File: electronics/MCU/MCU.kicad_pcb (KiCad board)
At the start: 2 copper layers, 77.5 x 26 mm, 46 parts, among them J1 UART, J10 Conn_01x09, J11 Button, J12 Power, J2 Conn_01x01, J3 Conn_01x01, J4 Conn_01x01, J5 Conn_01x01, J6 Conn_01x01, J7 Conn_01x01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

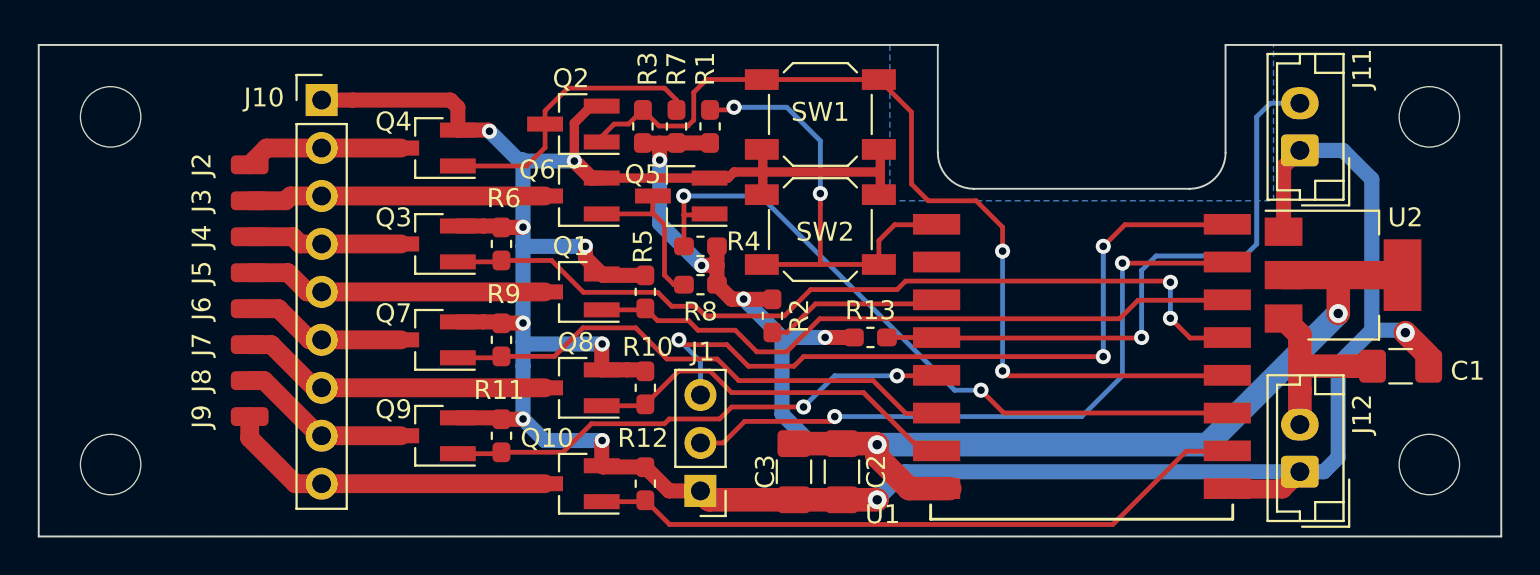
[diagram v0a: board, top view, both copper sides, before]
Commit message: Relay board ready, ESP3266 redesign (GPIO16 instead of GPIO0)
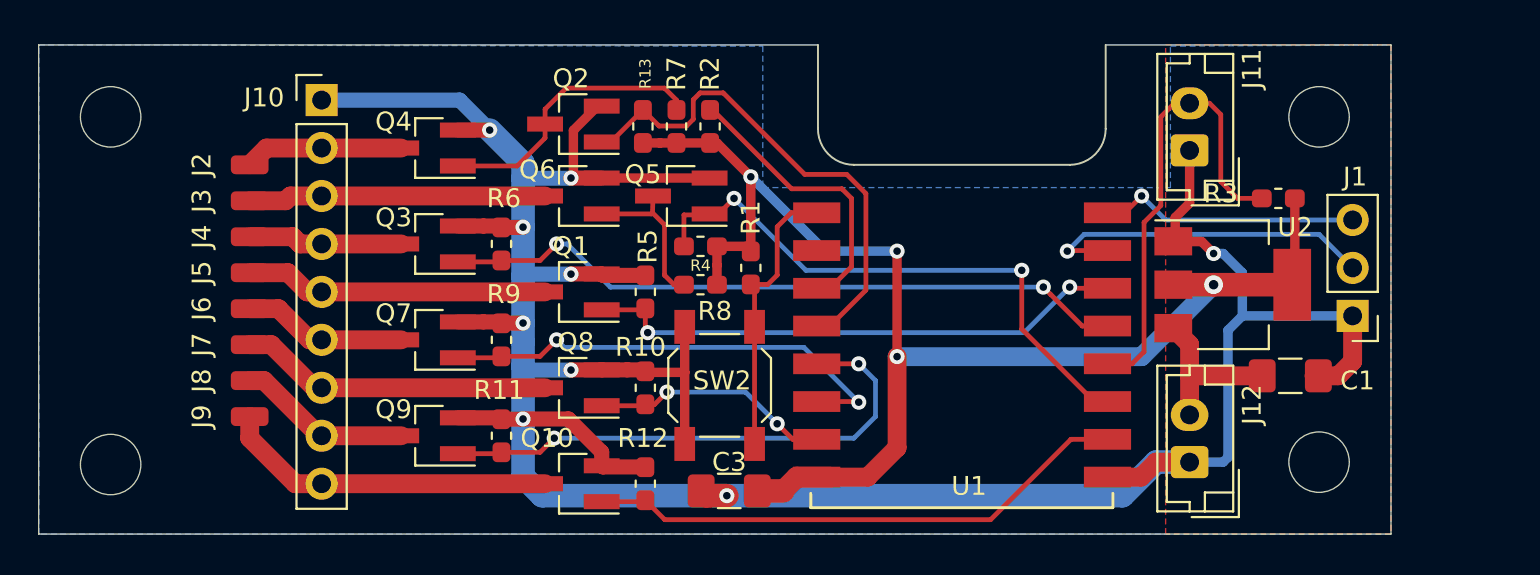
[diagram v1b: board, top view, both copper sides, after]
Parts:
- removed C2: 100n, Capacitor_SMD:C_1206_3216Metric_Pad1.42x1.75mm_HandSolder
- removed SW1: Flash, Button_Switch_SMD:SW_SPST_SKQG_WithStem
- R13: value 1k -> 10k
- R7, R8: value 1k -> 3k3
- moved J1 35.8 mm to (85.1, 75.6)
- moved R3 33.9 mm to (81.2, 69.3), turned to 180 degrees
- moved R13 16.4 mm to (47.5, 65.5), turned to 90 degrees
- moved R2 10.6 mm to (51.1, 65.5), turned to 90 degrees
- moved SW2 9.83 mm to (51.6, 79.2), turned to 270 degrees
- moved R1 7.80 mm to (53.2, 73.0), turned to 270 degrees
- moved U1 6.38 mm to (57.4, 70.1)
- moved J12 5.86 mm to (76.5, 83.3)
- moved C1 5.86 mm to (81.8, 78.7)
- moved U2 5.86 mm to (78.7, 73.9)
- moved REF** 5.84 mm to (83.3, 83.3)
- moved J11 5.84 mm to (76.5, 66.8)
- moved REF** 5.84 mm to (83.3, 65.0)
- moved C3 3.58 mm to (52.1, 84.8), turned to 180 degrees
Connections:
- net Net-(R1-Pad2) renamed /RST
- J11 pad 2: Net-(J11-Pad2) -> /GPIO0
- Q2 pad 1: /GPIO0 -> /GPIO16
- R13 pad 2: Net-(J11-Pad2) -> /GPIO16
- U1 pad 4: Net-(J11-Pad2) -> /GPIO16
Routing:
- net Net-(J11-Pad2): track 33.1 -> 0.00 mm, vias 1 -> 0
- net /GPIO16: track 0.00 -> 26.4 mm
- net Net-(J1-Pad3): track 38.8 -> 14.6 mm, vias 3 -> 1
- net /GPIO0: track 48.7 -> 25.5 mm, vias 2 -> 0
- net Net-(J1-Pad2): track 34.7 -> 17.7 mm, vias 2 -> 1
- net /RST: track 24.8 -> 15.8 mm, vias 2 -> 0
- net /GPIO4: track 44.4 -> 35.9 mm
- net /GPIO13: track 21.0 -> 13.4 mm, vias 0 -> 2
- net +3V3: track 78.8 -> 71.8 mm, vias 6 -> 4
- net /GPIO2: track 36.9 -> 30.0 mm
- net /GPIO15: track 34.6 -> 28.3 mm
- net /GPIO5: track 34.6 -> 28.4 mm, vias 0 -> 2
- net Net-(R2-Pad2): track 10.1 -> 14.7 mm
- net /GPIO12: track 28.6 -> 24.5 mm, vias 0 -> 2
- net /5V_In: track 9.82 -> 8.80 mm
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- added copper zone on F.Cu, net GND
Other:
- board size 77.5 x 26 mm -> 71.6 x 25.9 mm
- net class GND: trace_width 0.8 -> 0.5
- net class Power: trace_width 0.8 -> 0.5

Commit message: MCU: GPIO3 instead if GPIO2
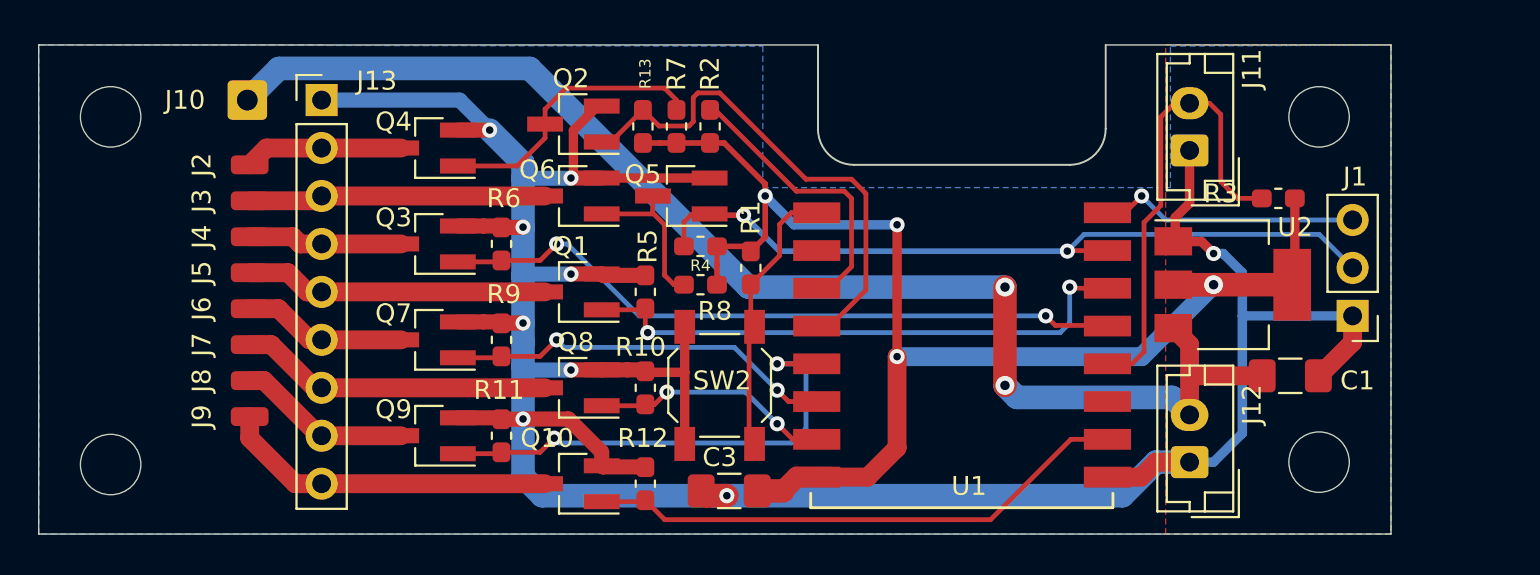
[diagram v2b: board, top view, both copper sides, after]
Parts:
- added J13: Relay +5V, Connector_Wire:SolderWire-0.5sqmm_1x01_D0.9mm_OD2.1mm, F.Cu at (26.5, 64.1)
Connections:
- net Net-(J1-Pad3) renamed /GPIO1
- J1 pad 2: Net-(J1-Pad2) -> /GPIO3
- Q5 pad 1: /GPIO2 -> /GPIO3
- R4 pad 2: /GPIO2 -> /GPIO3
- U1 pad 11: /GPIO2 -> (no net)
- U1 pad 15: Net-(J1-Pad2) -> /GPIO3
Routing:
- net /5V_In: track 8.80 -> 69.8 mm, vias 0 -> 2
- net /GPIO3: track 0.00 -> 40.3 mm, vias 0 -> 2
- net /GPIO2: track 30.0 -> 0.00 mm, vias 2 -> 0
- net Net-(J1-Pad2): track 17.7 -> 0.00 mm, vias 1 -> 0
- net /GPIO12: track 24.5 -> 21.5 mm
- net GND: track 160.6 -> 159.3 mm
- net /GPIO5: track 28.4 -> 29.5 mm
- net /GPIO14: track 27.6 -> 26.9 mm

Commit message: Small PCB modifications, esphome config added
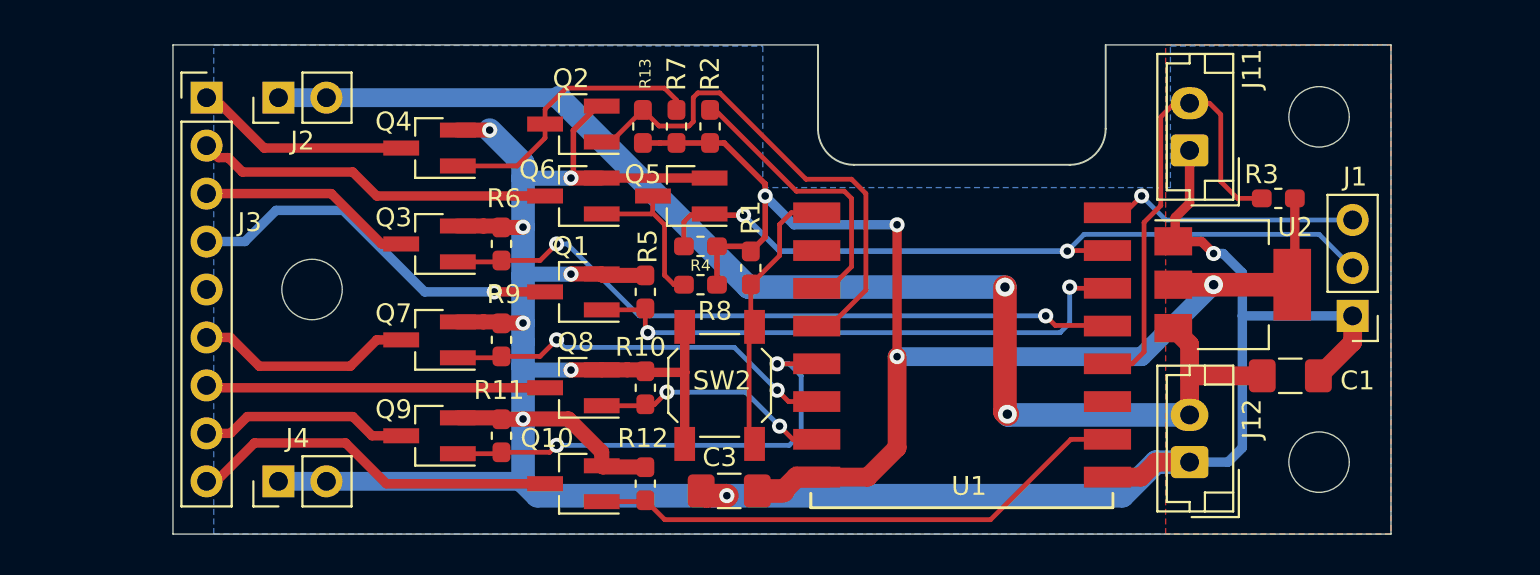
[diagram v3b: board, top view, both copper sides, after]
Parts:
- removed J10: Conn_01x09, Connector_PinHeader_2.54mm:PinHeader_1x09_P2.54mm_Vertical
- removed J13: Relay +5V, Connector_Wire:SolderWire-0.5sqmm_1x01_D0.9mm_OD2.1mm
- removed J5, J6, J7, J8, J9: Conn_01x01, Connector_Wire:SolderWirePad_1x01_SMD_1x2mm
- removed the REF** at (19.3, 83.4)
- J2: value Conn_01x01 -> Relay +5V; footprint Connector_Wire:SolderWirePad_1x01_SMD_1x2mm -> Connector_PinHeader_2.54mm:PinHeader_1x02_P2.54mm_Vertical
- J3: value Conn_01x01 -> Conn_01x09; footprint Connector_Wire:SolderWirePad_1x01_SMD_1x2mm -> Connector_PinHeader_2.54mm:PinHeader_1x09_P2.54mm_Vertical
- J4: value Conn_01x01 -> GND; footprint Connector_Wire:SolderWirePad_1x01_SMD_1x2mm -> Connector_PinHeader_2.54mm:PinHeader_1x02_P2.54mm_Vertical
- moved REF** 14.1 mm to (30.0, 74.2)
- moved J4 13.0 mm to (28.2, 84.3)
- moved J3 5.92 mm to (24.4, 64.0), turned to 0 degrees
- moved J2 3.87 mm to (28.2, 64.0)
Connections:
- C1 pad 1: /5V_In -> /+5V
- J12 pad 2: /5V_In -> /+5V
- J2 pad 1: /RELAY1 -> /+5V
- J3 pad 1: /RELAY2 -> /RELAY1
- J4 pad 1: /RELAY3 -> GND
- U2 pad 3: /5V_In -> /+5V
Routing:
- net /5V_In: track 69.8 -> 0.00 mm, vias 2 -> 0
- net /+5V: track 0.00 -> 67.9 mm, vias 0 -> 2
- net /RELAY4: track 16.1 -> 20.4 mm, vias 0 -> 1
- net GND: track 159.3 -> 163.3 mm
- net /RELAY2: track 15.8 -> 19.0 mm
- net /RELAY3: track 8.18 -> 11.4 mm
- net /RELAY1: track 8.39 -> 11.4 mm
- net /RELAY5: track 8.71 -> 11.5 mm
- net /RELAY8: track 17.8 -> 19.7 mm
- net /RELAY7: track 9.23 -> 11.1 mm
- net /RELAY6: track 16.6 -> 18.0 mm
- net /GPIO14: track 26.9 -> 26.0 mm
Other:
- board size 71.6 x 25.9 mm -> 64.5 x 25.9 mm
- net class Relay: trace_width 1 -> 0.5

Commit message: MCU: removed pullup from CH_PD (direct 3.3V)      improved clearance around the antenna added FreeCad design for case (uncompressed)
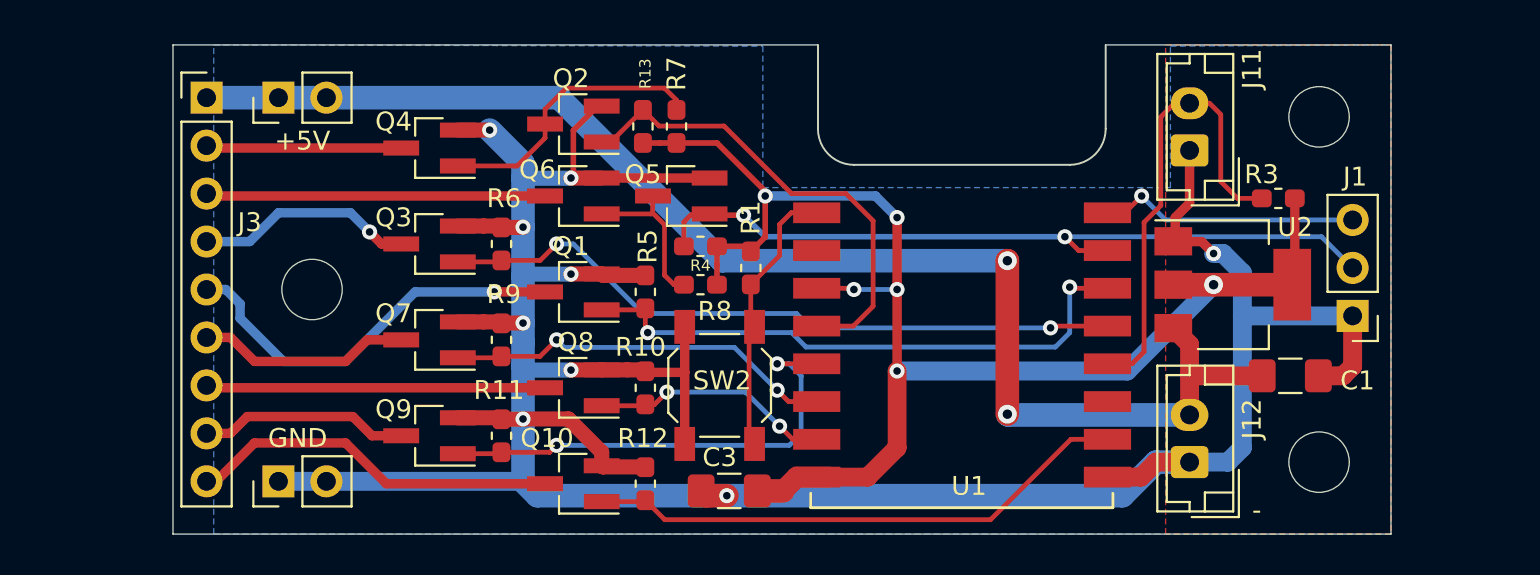
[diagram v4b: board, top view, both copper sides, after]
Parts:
- removed R2: 10k, Resistor_SMD:R_0603_1608Metric_Pad1.05x0.95mm_HandSolder
- renumbered J2 to +5V, J4 to GND
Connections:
- J3 pad 1: /RELAY1 -> /+5V
- J3 pad 2: /RELAY2 -> /RELAY1
- J3 pad 3: /RELAY3 -> /RELAY2
- J3 pad 4: /RELAY4 -> /RELAY3
- J3 pad 5: (no net) -> /RELAY4
- U1 pad 3: Net-(R2-Pad2) -> +3V3
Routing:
- net Net-(R2-Pad2): track 14.7 -> 0.00 mm
- net /+5V: track 67.9 -> 72.6 mm
- net +3V3: track 72.2 -> 76.1 mm, vias 4 -> 6
- net /GPIO16: track 26.5 -> 24.8 mm
- net /RELAY4: track 20.4 -> 21.5 mm
- net /RELAY1: track 11.4 -> 10.4 mm
- net /RELAY2: track 19.0 -> 18.0 mm
- net /GPIO5: track 29.5 -> 30.4 mm
- net GND: track 163.3 -> 164.0 mm
- net /RELAY3: track 11.4 -> 11.6 mm, vias 0 -> 1
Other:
- board text added: "-"
- board text added: "8 channel WiFi relay controller v1.0"

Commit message: PCB 1st batch
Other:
- outline, holes or cut-outs redrawn
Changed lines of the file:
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@@
   (general
     (thickness 1.6)
-    (drawings 16)
+    (drawings 17)
     (tracks 315)
     (zones 0)
@@
     (add_net "Net-(Q2-Pad3)")
     (add_net "Net-(Q5-Pad3)")
-    (add_net "Net-(R2-Pad2)")
-    (add_net "Net-(U1-Pad11)")
-    (add_net "Net-(U1-Pad2)")
   )
   (net_class GND ""
@@
     )
   )
+  (dimension 7.366 (width 0.15) (layer Dwgs.User)
+    (gr_text "7.366 mm" (at 26.289 54.326) (layer Dwgs.User)
+      (effects (font (size 1 1) (thickness 0.15)))
+    )
+    (feature1 (pts (xy 29.972 61.214) (xy 29.972 55.039579)))
+    (feature2 (pts (xy 22.606 61.214) (xy 22.606 55.039579)))
+    (crossbar (pts (xy 22.606 55.626) (xy 29.972 55.626)))
+    (arrow1a (pts (xy 29.972 55.626) (xy 28.845496 56.212421)))
+    (arrow1b (pts (xy 29.972 55.626) (xy 28.845496 55.039579)))
+    (arrow2a (pts (xy 22.606 55.626) (xy 23.732504 56.212421)))
+    (arrow2b (pts (xy 22.606 55.626) (xy 23.732504 55.039579)))
+  )
   (gr_text "8 channel WiFi\nrelay controller\nv1.0" (at 65.024 76.708 90) (layer B.SilkS)
     (effects (font (size 1 1) (thickness 0.15)) (justify mirror))
@@
     (arrow2b (pts (xy 90.678 65.024) (xy 91.264421 66.150504)))
   )
-  (gr_line (start 22.606 61.214) (end 56.769 61.214) (layer Edge.Cuts) (width 0.05))
+  (gr_line (start 22.606 61.214) (end 56.134 61.214) (layer Edge.Cuts) (width 0.05))
   (gr_line (start 87.122 87.122) (end 22.606 87.122) (layer Edge.Cuts) (width 0.05))
   (gr_line (start 87.122 61.214) (end 87.122 87.122) (layer Edge.Cuts) (width 0.05))
-  (gr_line (start 72.009 61.214) (end 87.122 61.214) (layer Edge.Cuts) (width 0.05))
-  (gr_arc (start 70.104 65.659) (end 70.104 67.564) (angle -90) (layer Edge.Cuts) (width 0.1))
-  (gr_arc (start 58.674 65.659) (end 56.769 65.659) (angle -90) (layer Edge.Cuts) (width 0.1))
-  (gr_line (start 56.769 61.214) (end 56.769 65.659) (layer Edge.Cuts) (width 0.1))
+  (gr_line (start 72.644 61.214) (end 87.122 61.214) (layer Edge.Cuts) (width 0.05))
+  (gr_arc (start 70.739 65.659) (end 70.739 67.564) (angle -90) (layer Edge.Cuts) (width 0.1))
+  (gr_arc (start 58.039 65.659) (end 56.134 65.659) (angle -90) (layer Edge.Cuts) (width 0.1))
+  (gr_line (start 56.134 61.214) (end 56.134 65.659) (layer Edge.Cuts) (width 0.1))
   (gr_line (start 22.606 87.122) (end 22.606 61.214) (layer Edge.Cuts) (width 0.05))
-  (gr_line (start 72.009 65.659) (end 72.009 61.214) (layer Edge.Cuts) (width 0.1))
-  (gr_line (start 58.674 67.564) (end 70.104 67.564) (layer Edge.Cuts) (width 0.1))
+  (gr_line (start 72.644 65.659) (end 72.644 61.214) (layer Edge.Cuts) (width 0.1))
+  (gr_line (start 58.039 67.564) (end 70.739 67.564) (layer Edge.Cuts) (width 0.1))
   (segment (start 39.93 70.805) (end 40.005 70.88) (width 0.8) (layer F.Cu) (net 1))
   (segment (start 37.695 70.805) (end 39.05 70.805) (width 0.8) (layer F.Cu) (net 1))
@@
   (segment (start 60.959992 74.168) (end 60.959996 74.167996) (width 0.254) (layer B.Cu) (net 2))
   (segment (start 60.959996 78.485996) (end 60.959996 74.167996) (width 0.5) (layer F.Cu) (net 2))
-  (segment (start 53.975 69.215) (end 59.817 69.215) (width 0.5) (layer B.Cu) (net 2))
-  (segment (start 59.817 69.215) (end 60.96 70.358) (width 0.5) (layer B.Cu) (net 2))
   (segment (start 53.975 68.961) (end 53.975 69.215) (width 0.3) (layer F.Cu) (net 2))
   (segment (start 51.421 66.407) (end 53.975 68.961) (width 0.3) (layer F.Cu) (net 2))
   (segment (start 49.276 66.407) (end 51.421 66.407) (width 0.3) (layer F.Cu) (net 2))
+  (segment (start 55.118 70.358) (end 60.96 70.358) (width 0.5) (layer B.Cu) (net 2))
+  (segment (start 53.975 69.215) (end 55.118 70.358) (width 0.5) (layer B.Cu) (net 2))
   (segment (start 24.511 66.675) (end 24.384 66.548) (width 0.5) (layer F.Cu) (net 3))
   (segment (start 34.695 66.675) (end 24.511 66.675) (width 0.5) (layer F.Cu) (net 3))
@@
   (segment (start 33.655 71.755) (end 33.02 71.12) (width 0.5) (layer F.Cu) (net 5))
   (segment (start 34.695 71.755) (end 33.655 71.755) (width 0.5) (layer F.Cu) (net 5))
+  (segment (start 26.416 71.628) (end 24.384 71.628) (width 0.5) (layer B.Cu) (net 5))
+  (segment (start 27.94 70.104) (end 26.416 71.628) (width 0.5) (layer B.Cu) (net 5))
+  (segment (start 32.004 70.104) (end 27.94 70.104) (width 0.5) (layer B.Cu) (net 5))
   (segment (start 33.02 71.12) (end 32.004 70.104) (width 0.5) (layer B.Cu) (net 5))
-  (segment (start 32.004 70.104) (end 28.194 70.104) (width 0.5) (layer B.Cu) (net 5))
-  (segment (start 26.67 71.628) (end 24.384 71.628) (width 0.5) (layer B.Cu) (net 5))
-  (segment (start 28.194 70.104) (end 26.67 71.628) (width 0.5) (layer B.Cu) (net 5))
   (via (at 39.624 74.295) (size 0.8) (drill 0.4) (layers F.Cu B.Cu) (net 6))
   (segment (start 42.315 74.295) (end 39.624 74.295) (width 0.5) (layer F.Cu) (net 6))

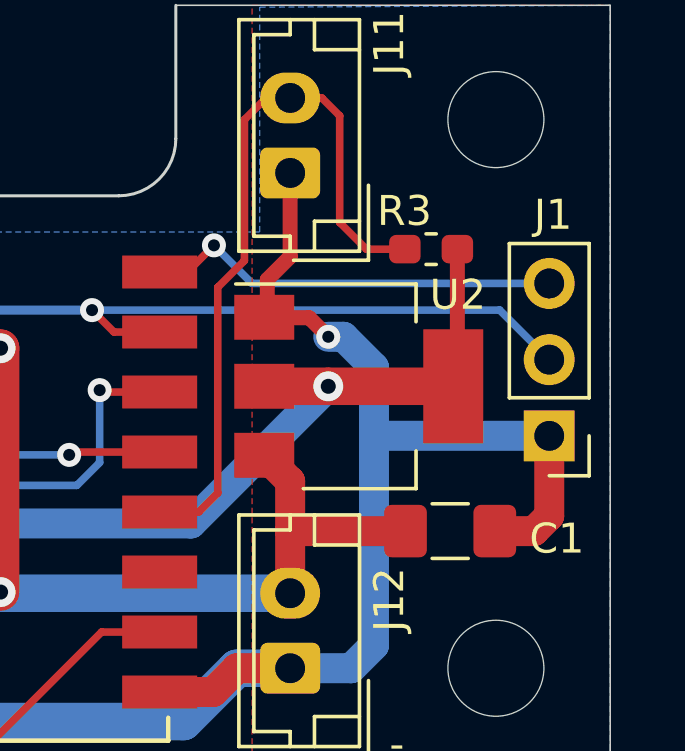
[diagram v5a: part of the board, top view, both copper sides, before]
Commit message: PCB: parts moved a bit away from the JST connectors
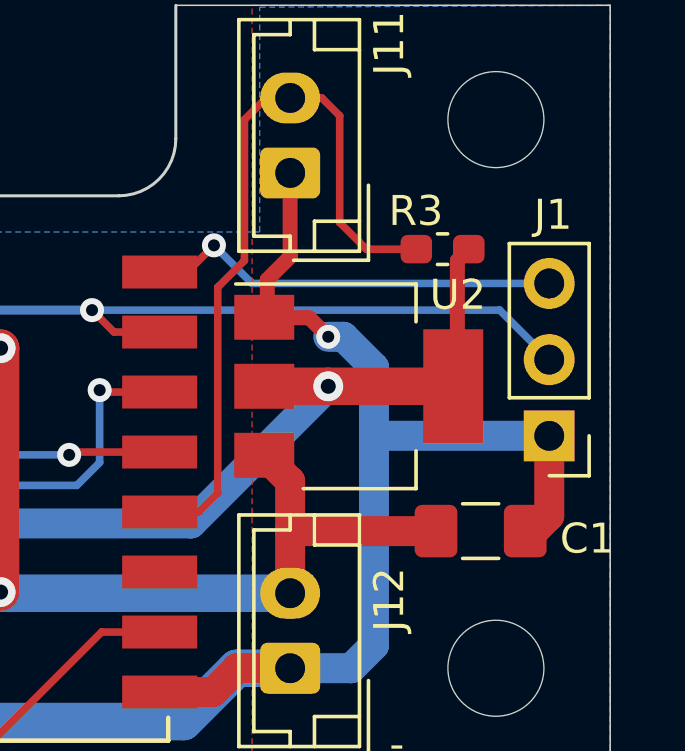
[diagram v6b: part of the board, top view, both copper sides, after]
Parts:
- moved C1 1.02 mm to (82.8, 78.7)
- moved R3 0.38 mm to (81.5, 69.3)
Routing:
- net /+5V: track 72.6 -> 73.6 mm
- net GND: track 164.0 -> 163.0 mm
